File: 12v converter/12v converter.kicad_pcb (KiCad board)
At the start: 2 copper layers, 88 x 51 mm, 14 parts, among them J1 Conn_01x02_Socket, J2 Conn_01x02_Socket, U1 LM2674N-3.3

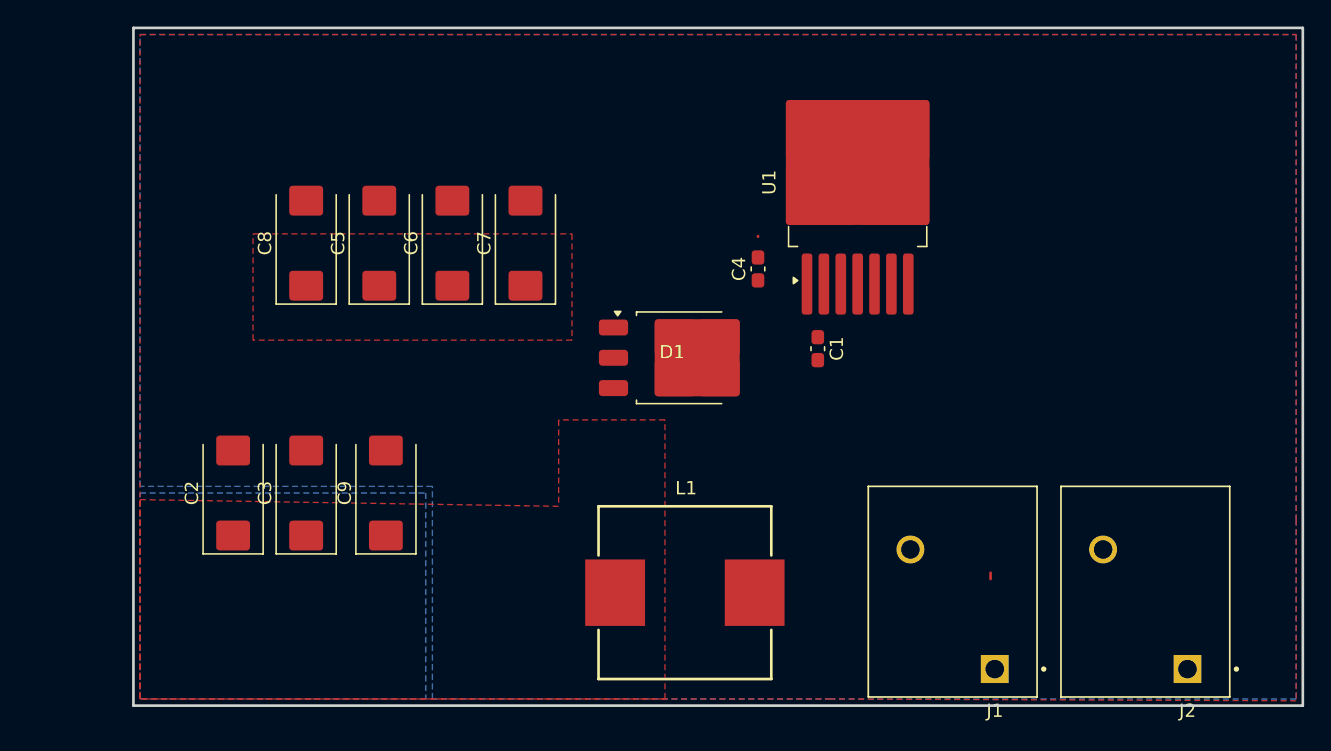
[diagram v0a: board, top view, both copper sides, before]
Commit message: Completed layout. Fixed incorrect schematic connections. Converted supermileage logo to silkscreen and added to layout
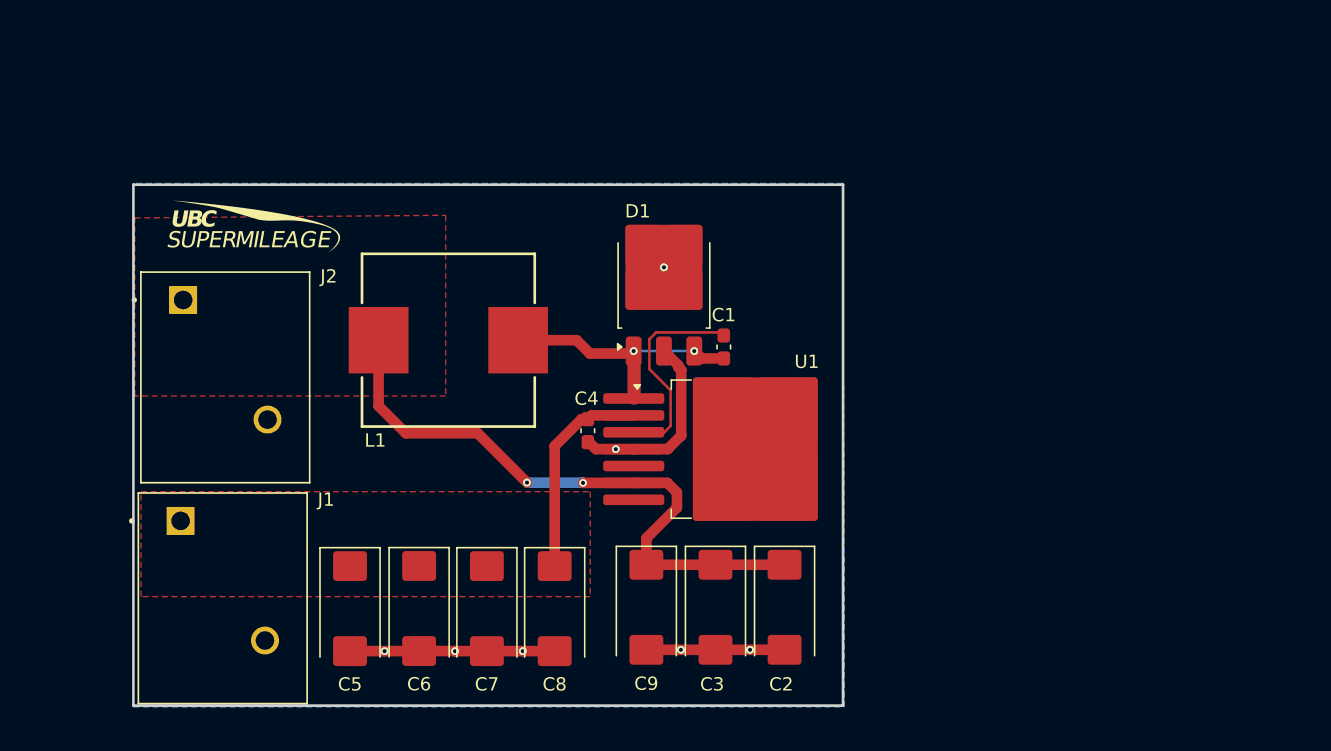
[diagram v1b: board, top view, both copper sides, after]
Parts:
- added G***: LOGO, fcp12vconv_footprints:sm_logo_small, F.Cu at (135.6, 94.5)
- moved J2 81.9 mm to (127.1, 113.7), turned to 0 degrees
- moved J1 69.6 mm to (126.9, 130.3), turned to 0 degrees
- moved C2 42.4 mm to (175.5, 123.1), turned to -90 degrees
- moved C8 33.3 mm to (158.2, 123.2), turned to -90 degrees
- moved C3 32.0 mm to (170.3, 123.1), turned to -90 degrees
- moved C7 27.7 mm to (153.1, 123.2), turned to -90 degrees
- moved C6 27.6 mm to (148.0, 123.2), turned to -90 degrees
- moved C5 27.6 mm to (142.8, 123.2), turned to -90 degrees
- moved L1 26.0 mm to (150.2, 103.0)
- moved U1 22.1 mm to (171.8, 111.2), turned to 0 degrees
- moved C9 21.4 mm to (165.1, 123.1), turned to -90 degrees
- moved C4 17.7 mm to (160.7, 109.8), turned to -90 degrees
- moved C1 7.08 mm to (170.9, 103.5)
- moved D1 5.02 mm to (166.5, 99.4), turned to 90 degrees
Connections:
- C1 pad 2: Net-(D1-K) -> /SW_OUT
- C2 pad 1: Net-(U1-FB) -> /VOUT
- C2 pad 2: Net-(D1-A) -> GND
- C3 pad 1: Net-(U1-FB) -> /VOUT
- C3 pad 2: Net-(D1-A) -> GND
- C9 pad 1: Net-(U1-FB) -> /VOUT
- C9 pad 2: Net-(D1-A) -> GND
- D1 pad 1: Net-(D1-K) -> /SW_OUT
- D1 pad 2: Net-(D1-A) -> GND
- L1 pad 1: Net-(U1-FB) -> /VOUT
- L1 pad 2: Net-(D1-K) -> /SW_OUT
- U1 pad 1: /VOUT -> /SW_OUT
- U1 pad 6: Net-(U1-FB) -> /VOUT
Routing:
- net /VOUT: track 0.00 -> 49.2 mm, vias 0 -> 2
- net GND: track 0.48 -> 40.4 mm, vias 0 -> 7
- net /SW_OUT: track 0.00 -> 19.8 mm, vias 0 -> 2
- net Net-(U1-CB): track 0.00 -> 16.1 mm
- net VIN: track 0.06 -> 15.9 mm
- removed copper zone on B.Cu, net /VOUT
- removed copper zone on F.Cu, net GND
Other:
- board size 88 x 51 mm -> 53.4 x 39.2 mm

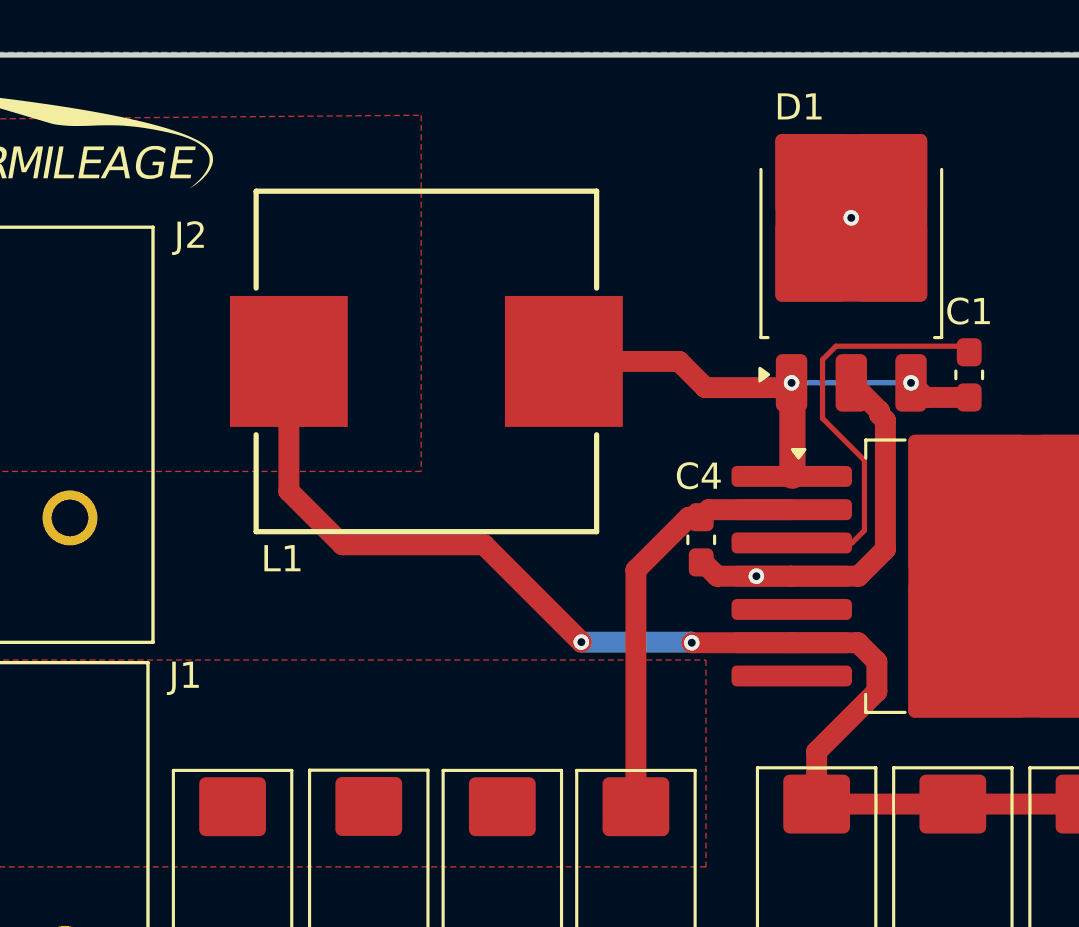
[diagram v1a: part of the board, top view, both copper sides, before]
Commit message: silkscreen labels for i/o and vias for diode
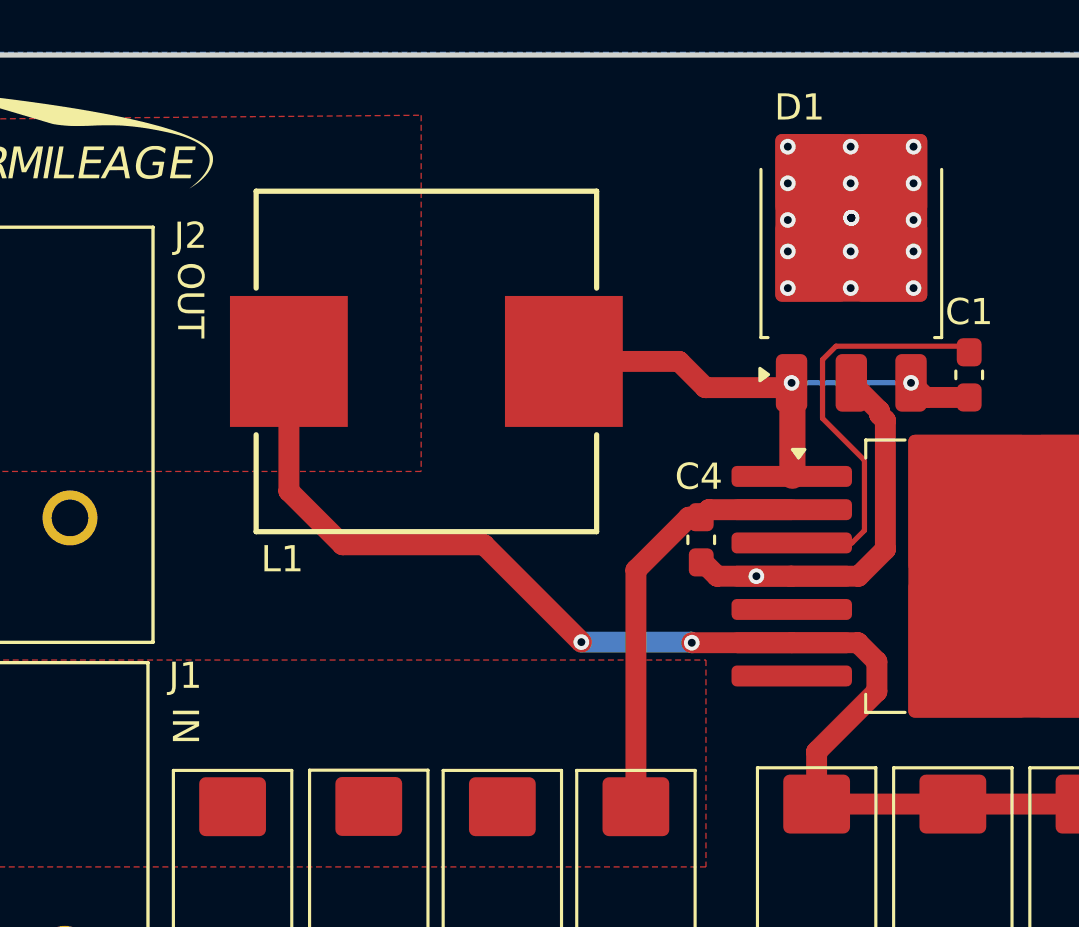
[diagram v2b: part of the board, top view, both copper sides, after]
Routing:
- net GND: vias 7 -> 23
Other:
- board text added: "IN"
- board text added: "OUT"
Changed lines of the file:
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@@
 		(tags "D2PAK DDPAK TO-263 D2PAK-7 TO-263-7 SOT-427")
 		(property "Reference" "U1"
-			(at 5.375 -6.575 360)
+			(at 5.375 -6.575 0)
 			(layer "F.SilkS")
 			(effects
@@
 		)
 		(property "Value" "LM2674N-3.3"
-			(at 0 6.65 360)
+			(at 0 6.65 0)
 			(layer "F.Fab")
 			(hide yes)
@@
 		)
 		(fp_text user "${REFERENCE}"
-			(at 0 0 360)
+			(at 0 0 0)
 			(layer "F.Fab")
 			(effects
@@
 		(at 126.87 130.35)
 		(property "Reference" "J1"
-			(at 14.13 -15.35 360)
+			(at 14.13 -15.35 0)
 			(layer "F.SilkS")
 			(effects
@@
 		)
 		(property "Value" "Conn_01x02_Socket"
-			(at 4 -18.25 360)
+			(at 4 -18.25 0)
 			(layer "F.Fab")
 			(effects
@@
 		)
 		(property "Footprint" "fcp12vconv_footprints:PHOENIX_1777545"
-			(at 0 0 360)
+			(at 0 0 0)
 			(layer "F.Fab")
 			(hide yes)
@@
 		)
 		(property "Datasheet" "https://mm.digikey.com/Volume0/opasdata/d220001/medias/docus/404/1777545.pdf"
-			(at 0 0 360)
+			(at 0 0 0)
 			(layer "F.Fab")
 			(hide yes)
@@
 		)
 		(property "Description" "Generic connector, single row, 01x02, script generated"
-			(at 0 0 360)
+			(at 0 0 0)
 			(layer "F.Fab")
 			(hide yes)
@@
 		(tags "capacitor tantalum")
 		(property "Reference" "C7"
-			(at 5.7 0 360)
+			(at 5.7 0 0)
 			(layer "F.SilkS")
 			(effects
@@
 		(descr "<b> <br><b>WE-HCI SMD Flat Wire High Current Inductor<br></b><pre> <b><font size=\"4\">Size: </b>1365")
 		(property "Reference" "L1"
-			(at -5.5 7.55 360)
+			(at -5.5 7.55 0)
 			(layer "F.SilkS")
 			(effects
@@
 		)
 		(property "Value" "33 uH"
-			(at 0 0 360)
+			(at 0 0 0)
 			(layer "F.Fab")
 			(effects
@@
 		)
 		(property "Footprint" "fcp12vconv_footprints:WE-HCI_1365"
-			(at 0 0 360)
+			(at 0 0 0)
 			(layer "F.Fab")
 			(hide yes)
@@
 		)
 		(property "Datasheet" "https://www.we-online.com/components/products/datasheet/7443551331.pdf"
-			(at 0 0 360)
+			(at 0 0 0)
 			(layer "F.Fab")
 			(hide yes)
@@
 		)
 		(property "Description" "Inductor"
-			(at 0 0 360)
+			(at 0 0 0)
 			(layer "F.Fab")
 			(hide yes)
@@
 		(tags "capacitor tantalum")
 		(property "Reference" "C5"
-			(at 5.7 0 360)
+			(at 5.7 0 0)
 			(layer "F.SilkS")
 			(effects
@@
 		(tags "capacitor tantalum")
 		(property "Reference" "C6"
-			(at 5.7 0 360)
+			(at 5.7 0 0)
 			(layer "F.SilkS")
 			(effects
@@
 		(at 127.0625 113.725)
 		(property "Reference" "J2"
-			(at 14.1375 -15.525 360)
+			(at 14.1375 -15.525 180)
 			(layer "F.SilkS")
 			(effects
@@
 		)
 		(property "Value" "Conn_01x02_Socket"
-			(at 4.5 -18.5 360)
+			(at 4.5 -18.5 0)
 			(layer "F.Fab")
 			(effects
@@
 		)
 		(property "Footprint" "fcp12vconv_footprints:PHOENIX_1777545"
-			(at 0 0 360)
+			(at 0 0 0)
 			(layer "F.Fab")
 			(hide yes)
@@
 		)
 		(property "Datasheet" "https://mm.digikey.com/Volume0/opasdata/d220001/medias/docus/404/1777545.pdf"
-			(at 0 0 360)
+			(at 0 0 0)
 			(layer "F.Fab")
 			(hide yes)
@@
 		)
 		(property "Description" "Generic connector, single row, 01x02, script generated"
-			(at 0 0 360)
+			(at 0 0 0)
 			(layer "F.Fab")
 			(hide yes)
@@
 		(tags "capacitor handsolder")
 		(property "Reference" "C4"
-			(at -2.41 0.093884 360)
+			(at -2.41 0.093884 0)
 			(layer "F.SilkS")
 			(effects
@@
 		(tags "capacitor handsolder")
 		(property "Reference" "C1"
-			(at -2.4 0 360)
+			(at -2.4 0 0)
 			(layer "F.SilkS")
 			(effects
@@
 		(tags "capacitor tantalum")
 		(property "Reference" "C8"
-			(at 5.7 0 360)
+			(at 5.7 0 0)
 			(layer "F.SilkS")
 			(effects
@@
 		(layer "Edge.Cuts")
 	)
+	(gr_text "OUT"
+		(at 140.6 99.2 -90)
+		(layer "F.SilkS")
+		(effects
+			(font
+				(size 1 1)
+				(thickness 0.1)
+			)
+			(justify left bottom)
+		)
+	)
+	(gr_text "IN"
+		(at 140.4 116.2 -90)
+		(layer "F.SilkS")
+		(effects
+			(font
+				(size 1 1)
+				(thickness 0.1)
+			)
+			(justify left bottom)
+		)
+	)
 	(segment
 		(start 165.325 105.175)
@@
 	)
 	(via
+		(at 164 98.8)
+		(size 0.6)
+		(drill 0.3)
+		(layers "F.Cu" "B.Cu")
+		(net 3)
+	)
+	(via
+		(at 168.8 100.2)
+		(size 0.6)
+		(drill 0.3)
+		(layers "F.Cu" "B.Cu")
+		(net 3)
+	)
+	(via
 		(at 145.4 126.4)
 		(size 0.6)
@@
 	)
 	(via
+		(at 164 94.8)
+		(size 0.6)
+		(drill 0.3)
+		(layers "F.Cu" "B.Cu")
+		(net 3)
+	)
+	(via
 		(at 166.423221 97.518559)
 		(size 0.6)
@@
 	)
 	(via
+		(at 166.4 94.8)
+		(size 0.6)
+		(drill 0.3)
+		(layers "F.Cu" "B.Cu")
+		(net 3)
+	)
+	(via
+		(at 168.8 98.8)
+		(size 0.6)
+		(drill 0.3)
+		(layers "F.Cu" "B.Cu")
+		(net 3)
+	)
+	(via
 		(at 150.7 126.4)
 		(size 0.6)
@@
 	)
 	(via
+		(at 164 96.2)
+		(size 0.6)
+		(drill 0.3)
+		(layers "F.Cu" "B.Cu")
+		(net 3)
+	)
+	(via
 		(at 172.9 126.3)
 		(size 0.6)
@@
 	)
 	(via
+		(at 166.4 96.2)
+		(size 0.6)
+		(drill 0.3)
+		(layers "F.Cu" "B.Cu")
+		(net 3)
+	)
+	(via
 		(at 167.7 126.3)
 		(size 0.6)
@@
 	)
 	(via
+		(at 166.423221 97.518559)
+		(size 0.6)
+		(drill 0.3)
+		(layers "F.Cu" "B.Cu")
+		(net 3)
+	)
+	(via
+		(at 168.8 97.6)
+		(size 0.6)
+		(drill 0.3)
+		(layers "F.Cu" "B.Cu")
+		(net 3)
+	)
+	(via
 		(at 162.8 111.2)
 		(size 0.6)
@@
 	)
 	(via
+		(at 166.423221 97.518559)
+		(size 0.6)
+		(drill 0.3)
+		(layers "F.Cu" "B.Cu")
+		(net 3)
+	)
+	(via
+		(at 164 100.2)
+		(size 0.6)
+		(drill 0.3)
+		(layers "F.Cu" "B.Cu")
+		(net 3)
+	)
+	(via
 		(at 155.8 126.4)
 		(size 0.6)
@@
 		(net 3)
 	)
+	(via
+		(at 164 97.6)
+		(size 0.6)
+		(drill 0.3)
+		(layers "F.Cu" "B.Cu")
+		(net 3)
+	)
+	(via
+		(at 168.8 96.2)
+		(size 0.6)
+		(drill 0.3)
+		(layers "F.Cu" "B.Cu")
+		(net 3)
+	)
+	(via
+		(at 166.4 100.2)
+		(size 0.6)
+		(drill 0.3)
+		(layers "F.Cu" "B.Cu")
+		(net 3)
+	)
+	(via
+		(at 166.4 98.8)
+		(size 0.6)
+		(drill 0.3)
+		(layers "F.Cu" "B.Cu")
+		(net 3)
+	)
+	(via
+		(at 168.8 94.8)
+		(size 0.6)
+		(drill 0.3)
+		(layers "F.Cu" "B.Cu")
+		(net 3)
+	)
 	(segment
 		(start 160.981383 108.66)
@@
 		(polygon
 			(pts
-				(xy 126.5 91.2) (xy 126.5 130.6) (xy 180 130.6) (xy 179.9 91.2) (xy 179.9 91.2)
+				(xy 126.5 91.2) (xy 126.5 130.6) (xy 180 130.6) (xy 179.9 91.2)
 			)
 		)

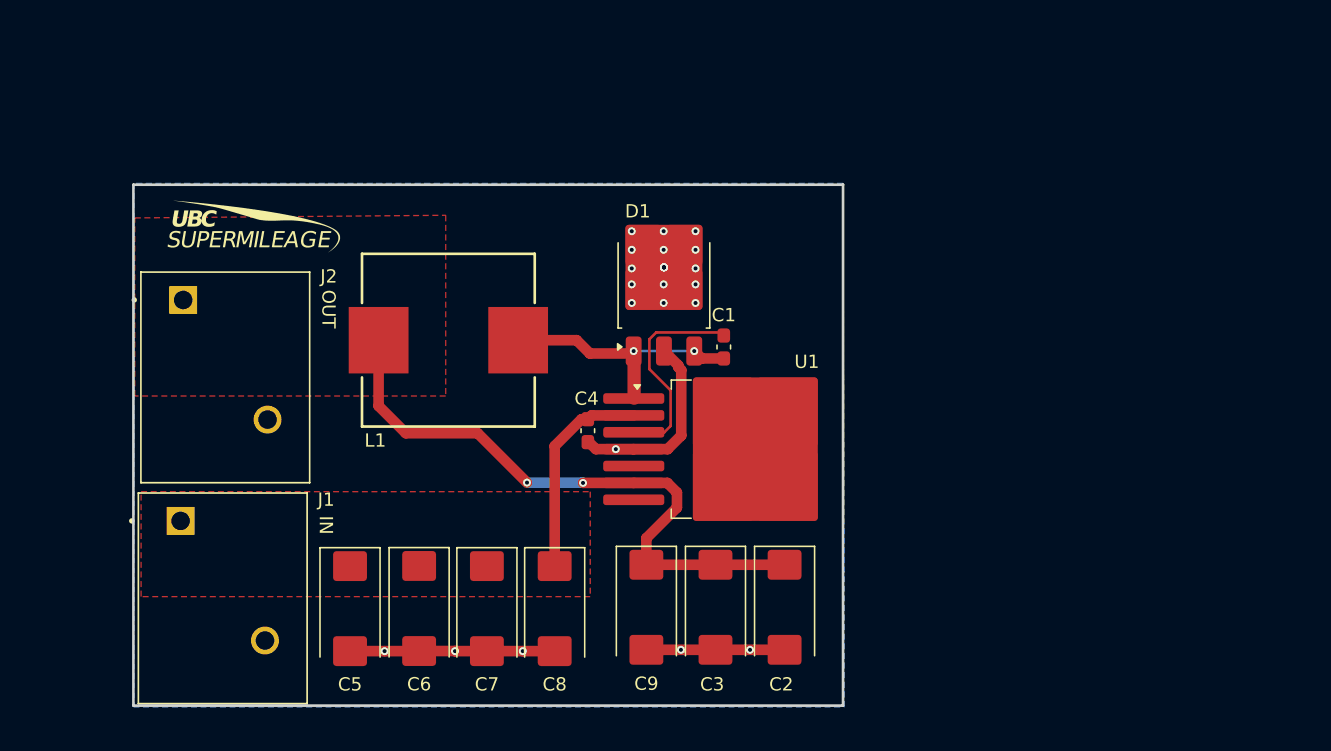
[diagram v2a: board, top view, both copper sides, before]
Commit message: test points, labels
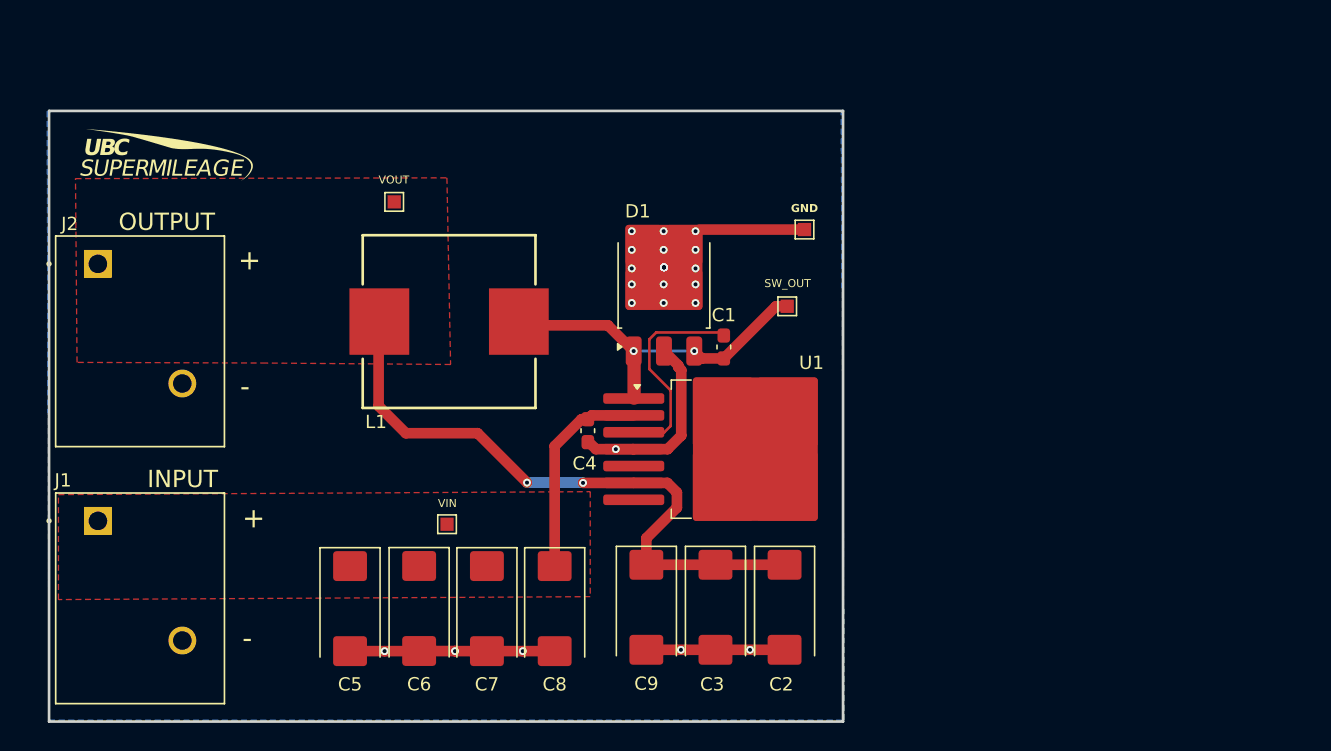
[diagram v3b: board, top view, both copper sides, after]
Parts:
- added GND: GND, TestPoint:TestPoint_Pad_1.0x1.0mm, F.Cu at (177.0, 94.7)
- added SW_OUT: switch_output, TestPoint:TestPoint_Pad_1.0x1.0mm, F.Cu at (175.7, 100.5)
- added VIN: VIN, TestPoint:TestPoint_Pad_1.0x1.0mm, F.Cu at (150.1, 116.8)
- added VOUT: VOUT, TestPoint:TestPoint_Pad_1.0x1.0mm, F.Cu at (146.1, 92.6)
- moved G*** 8.49 mm to (129.0, 89.1)
- moved J2 6.97 mm to (120.6, 111.0)
- moved J1 6.22 mm to (120.7, 130.3)
- moved L1 1.40 mm to (150.3, 101.6)
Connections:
- C2 pad 1: /VOUT -> Net-(U1-FB)
- C3 pad 1: /VOUT -> Net-(U1-FB)
- C9 pad 1: /VOUT -> Net-(U1-FB)
- L1 pad 1: /VOUT -> Net-(U1-FB)
- U1 pad 6: /VOUT -> Net-(U1-FB)
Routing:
- net Net-(U1-FB): track 0.00 -> 50.6 mm, vias 0 -> 2
- net /VOUT: track 49.2 -> 0.00 mm, vias 2 -> 0
- net GND: track 40.4 -> 53.6 mm
- net /SW_OUT: track 19.8 -> 26.7 mm
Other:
- board size 53.4 x 39.2 mm -> 59.8 x 46 mm
- board text added: "+"
- board text added: "-"
- board text added: "INPUT"
- board text added: "OUTPUT"
- board text removed: "IN"
- board text removed: "OUT"

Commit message: rearrangmenet, silkscreen stuff
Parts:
- moved J1 15.8 mm to (119.0, 114.6), turned to -90 degrees
- moved J2 14.4 mm to (119.0, 96.7), turned to -90 degrees
- moved VIN 7.86 mm to (142.2, 116.8)
- moved VOUT 6.33 mm to (139.8, 92.4)
- moved L1 0.83 mm to (150.3, 100.8)
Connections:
- C2 pad 1: Net-(U1-FB) -> /VOUT
- C3 pad 1: Net-(U1-FB) -> /VOUT
- C9 pad 1: Net-(U1-FB) -> /VOUT
- L1 pad 1: Net-(U1-FB) -> /VOUT
- U1 pad 6: Net-(U1-FB) -> /VOUT
- VOUT pad 1: Net-(U1-FB) -> /VOUT
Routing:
- net Net-(U1-FB): track 50.6 -> 0.00 mm, vias 2 -> 0
- net /VOUT: track 0.00 -> 50.6 mm, vias 0 -> 2
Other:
- board size 59.8 x 46 mm -> 61.3 x 46 mm
- board text added: "EMMA YU VOLTAGE DOWN I'M UP SHELL ECOMARATHON 2025"
